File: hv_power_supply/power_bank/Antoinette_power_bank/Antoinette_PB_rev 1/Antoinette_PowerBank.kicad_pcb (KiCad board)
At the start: 2 copper layers, 30.5 x 48.3 mm, 44 parts, among them J1 NanoFit_RA_TH_02, J2 USB-Micro-1981568-1, J3 NanoFit_RA_TH_02, J4 USB-A-S-X-X-SM2, J5 NanoFit_RA_TH_02, Q1 SSM3K333R, U2 MCP73871T-2CCI_ML, U3 TPS61090RSAR

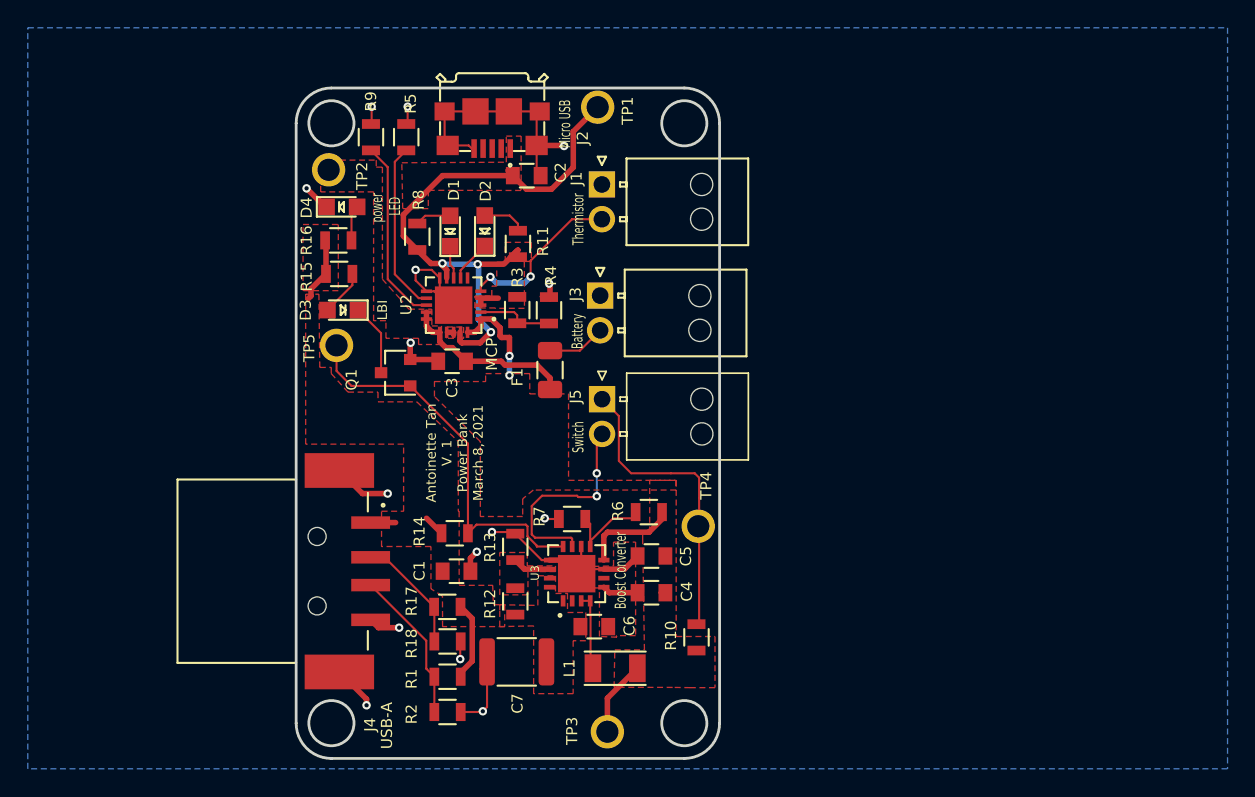
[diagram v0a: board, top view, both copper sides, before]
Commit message: UpdMoved USB-A in, and updated traces
Moved USB-A in, replaced copper pours with traces, added mounting holes
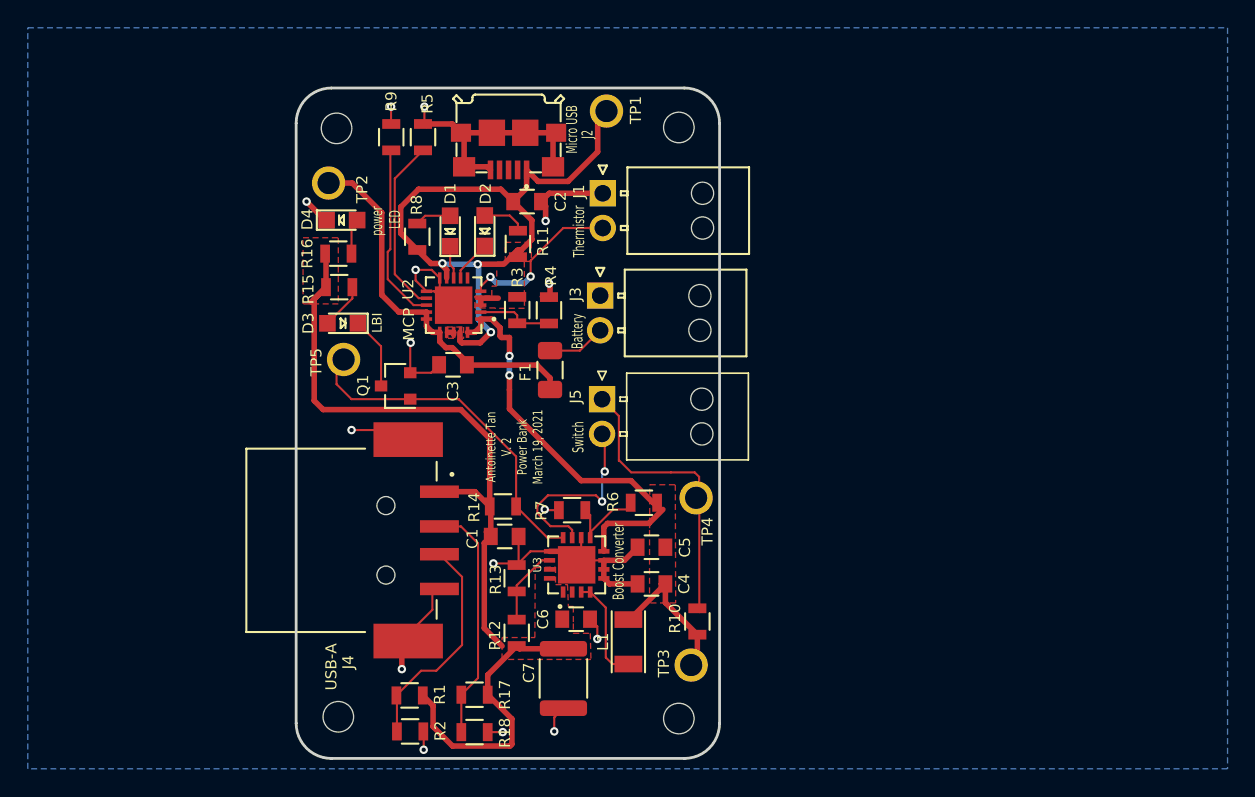
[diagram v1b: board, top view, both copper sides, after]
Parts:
- added R: MountingHole_2.2mm_M2, formula:MountingHole_2.2mm_M2, F.Cu at (97.7, 75.1)
- added REF**: MountingHole_2.2mm_M2, formula:MountingHole_2.2mm_M2, F.Cu at (73.2, 75.0)
- added REF**: MountingHole_2.2mm_M2, formula:MountingHole_2.2mm_M2, F.Cu at (97.7, 32.6)
- added REF**: MountingHole_2.2mm_M2, formula:MountingHole_2.2mm_M2, F.Cu at (73.0, 32.6)
- moved TP3 7.71 mm to (98.6, 71.3)
- moved R18 6.81 mm to (83.0, 76.1)
- moved R17 6.62 mm to (83.0, 73.4)
- moved J4 5.43 mm to (76.6, 62.3)
- moved C1 4.28 mm to (85.1, 62.0)
- moved R14 3.97 mm to (85.0, 59.9)
- moved C7 3.57 mm to (89.4, 72.2), turned to 270 degrees
- moved R1 3.04 mm to (78.3, 73.5)
- moved R2 3.03 mm to (78.3, 76.0)
- moved R13 2.26 mm to (86.0, 65.0)
- moved R12 2.26 mm to (86.0, 69.0)
- moved L1 2.13 mm to (94.0, 69.6), turned to 270 degrees
- moved TP4 2.05 mm to (98.9, 59.2)
- moved J2 1.94 mm to (85.4, 33.0)
- moved C2 1.87 mm to (86.7, 37.9)
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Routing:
- net +5V: track 15.9 -> 68.0 mm
- net +BATT: track 19.6 -> 40.1 mm
- net /Battery+: track 12.7 -> 26.9 mm
- net Net-(J4-Pad02): track 9.27 -> 18.9 mm
- net Net-(J4-Pad03): track 11.3 -> 17.6 mm
- net VBUS: track 44.4 -> 50.3 mm
- net GND: track 75.0 -> 80.5 mm
- net Net-(Q1-Pad1): track 28.1 -> 24.8 mm
- net Net-(R12-Pad2): track 2.74 -> 5.57 mm
- net Net-(L1-Pad2): track 4.93 -> 7.71 mm
- removed copper zone on F.Cu, net /Battery+
- removed copper zone on F.Cu, net GND
- removed copper zone on F.Cu, net Net-(R12-Pad2)
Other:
- outline, holes or cut-outs redrawn
- board text added: "Antoinette Tan V. 2 Power Bank March 19, 2021"
- board text removed: "Antoinette Tan V. 1 Power Bank March 8, 2021"

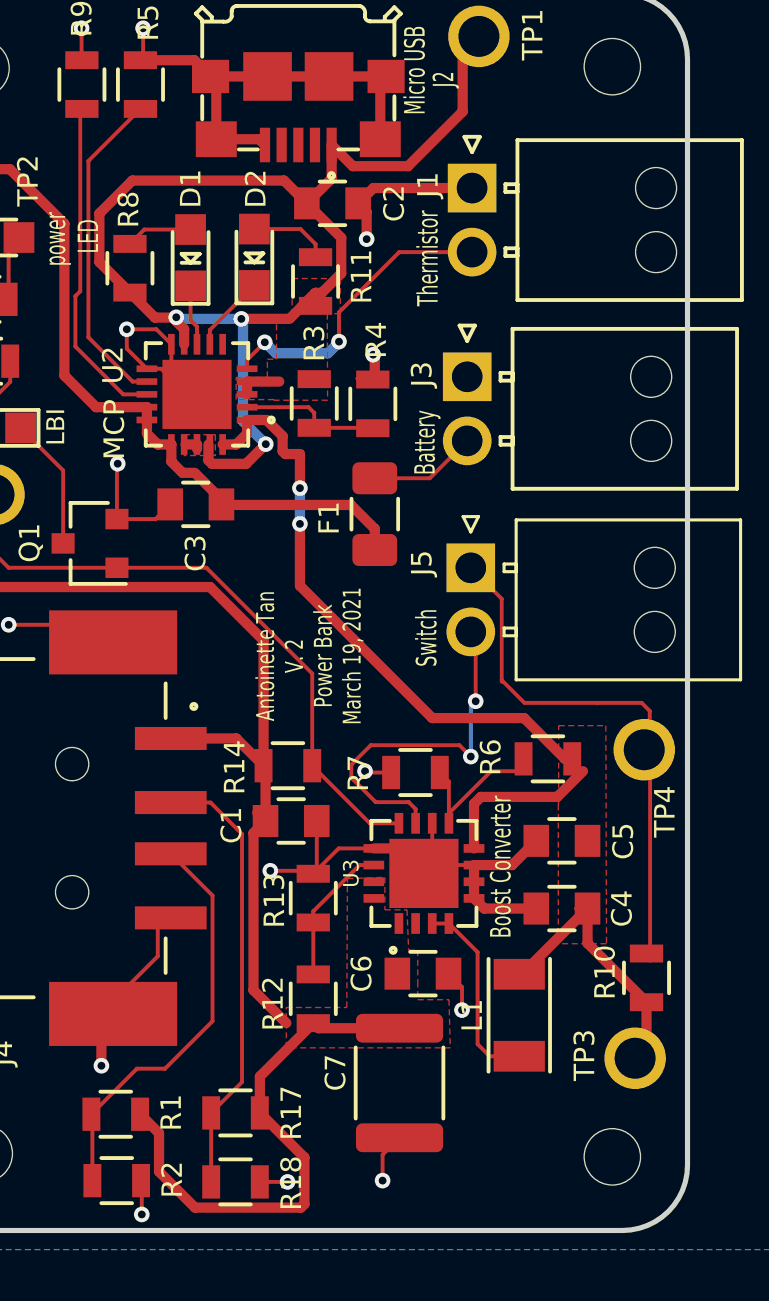
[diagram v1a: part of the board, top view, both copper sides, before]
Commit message: connect gnd to pw grnd
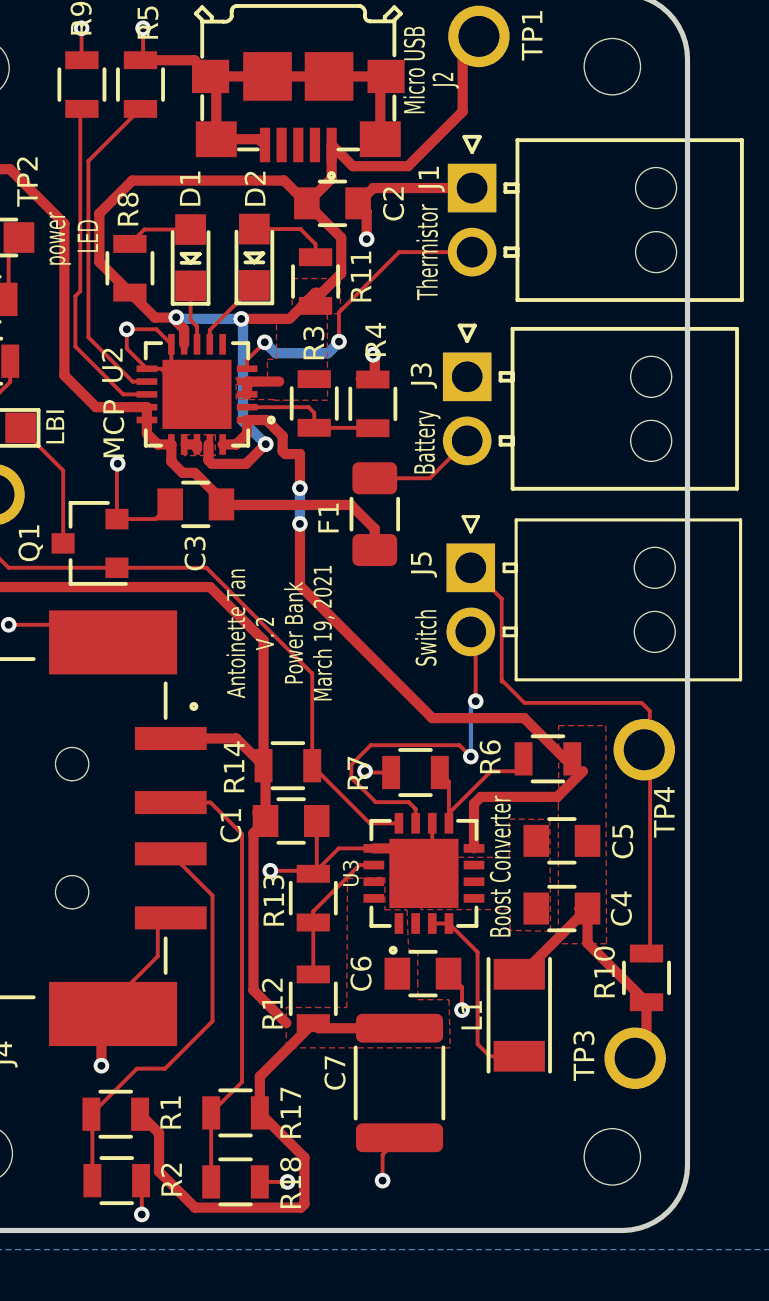
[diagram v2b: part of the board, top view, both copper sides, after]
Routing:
- net GND: track 80.5 -> 72.1 mm
- added copper zone on F.Cu, net GND

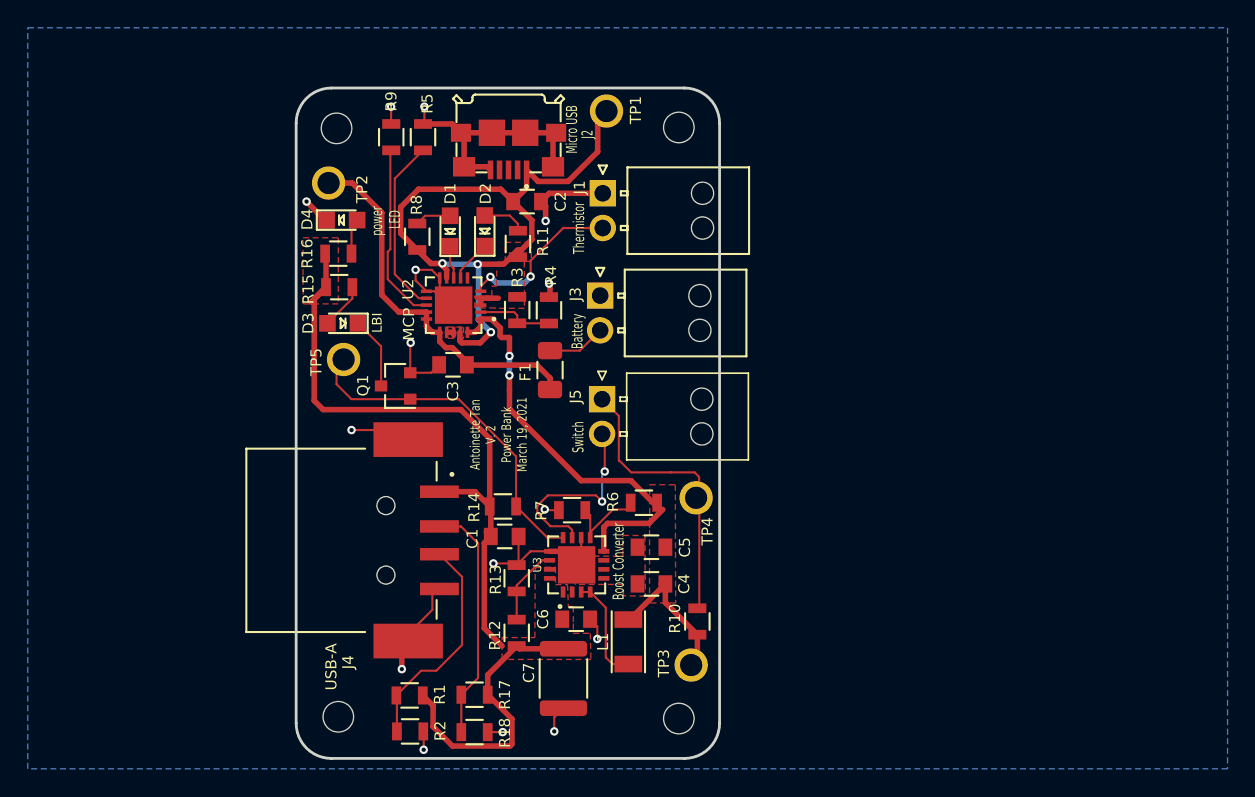
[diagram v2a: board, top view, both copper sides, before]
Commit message: Add updated PCB with new inductor.
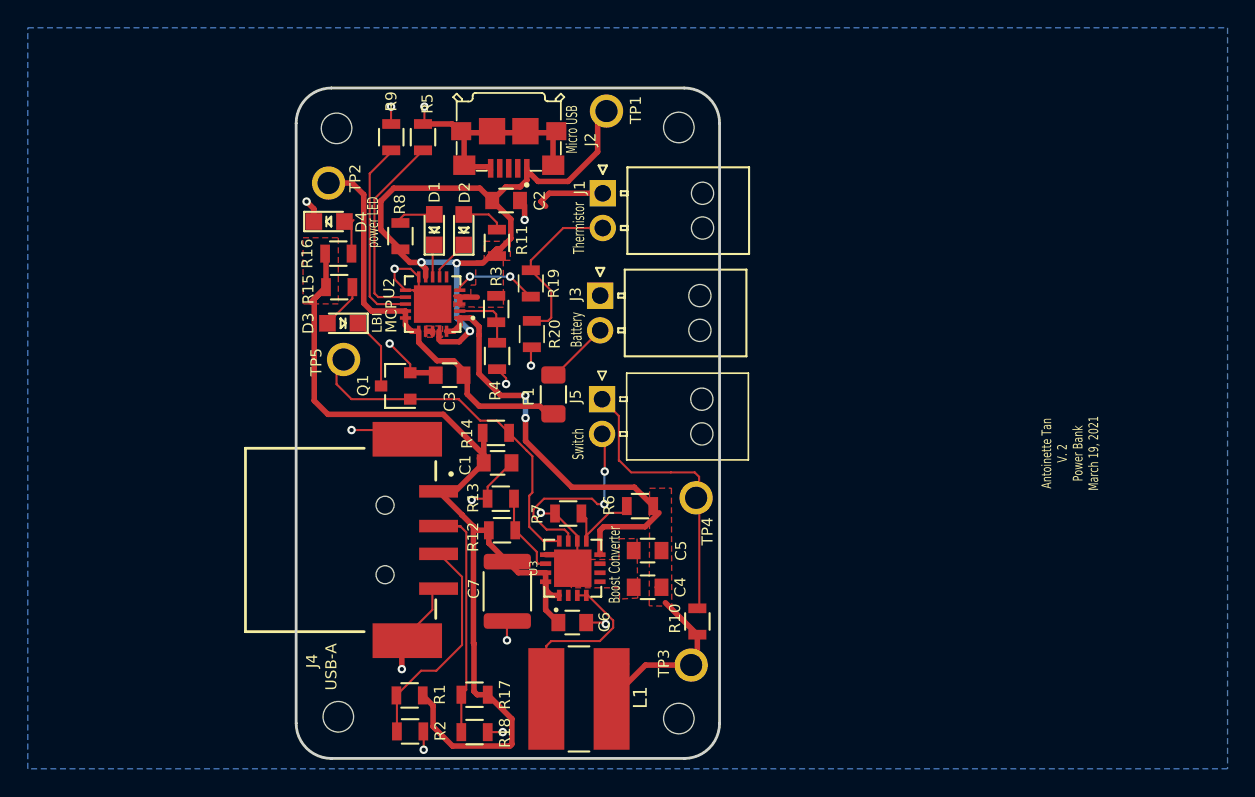
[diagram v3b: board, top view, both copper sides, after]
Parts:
- added R19: R_1.54K, footprints:R_0805_OEM, F.Cu at (87.0, 43.8)
- added R20: R_69.8K, footprints:R_0805_OEM, F.Cu at (87.1, 47.4)
- L1: value L_6.8uH -> L_10uH; footprint footprints:L_100uH_OEM -> footprints:BournsInductor
- moved C7 7.46 mm to (85.3, 66.0)
- moved R12 7.46 mm to (84.9, 61.6), turned to 0 degrees
- moved R13 5.84 mm to (84.8, 59.3), turned to 180 degrees
- moved L1 5.44 mm to (90.5, 73.7), turned to 0 degrees
- moved R14 5.32 mm to (84.5, 54.6)
- moved C1 5.32 mm to (84.6, 56.7)
- moved R4 4.97 mm to (84.6, 49.0), turned to 270 degrees
- moved F1 1.77 mm to (88.6, 51.8)
- moved C2 1.51 mm to (85.2, 37.8)
- moved R11 1.51 mm to (84.6, 40.9)
- moved U2 1.51 mm to (79.9, 45.3)
- moved D2 1.51 mm to (82.2, 39.9)
- moved R3 1.51 mm to (84.5, 45.6)
- moved R8 1.21 mm to (77.6, 40.4)
- moved D1 1.15 mm to (80.1, 39.9)
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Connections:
- J1 pad 2: /16KThermistor -> /10KThermistor
- L1 pad 1: +BATT -> Net-(L1-Pad1)
- L1 pad 2: Net-(L1-Pad2) -> +BATT
- U2 pad 5: /16KThermistor -> Net-(R19-Pad2)
- U3 pad 3: Net-(L1-Pad2) -> Net-(L1-Pad1)
- U3 pad 4: Net-(L1-Pad2) -> Net-(L1-Pad1)
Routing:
- net Net-(L1-Pad1): track 0.00 -> 13.1 mm
- net /10KThermistor: track 0.00 -> 12.4 mm
- net /16KThermistor: track 11.9 -> 0.00 mm, vias 2 -> 0
- net +5V: track 68.0 -> 76.1 mm
- net Net-(L1-Pad2): track 7.71 -> 0.00 mm
- net Net-(R19-Pad2): track 0.00 -> 6.38 mm, vias 0 -> 2
- net +BATT: track 40.1 -> 45.3 mm
- net /Battery+: track 26.9 -> 29.5 mm
- net GND: track 72.1 -> 73.5 mm, vias 15 -> 16
- net VBUS: track 50.3 -> 51.6 mm
- net Net-(R5-Pad1): track 12.8 -> 14.1 mm
- net Net-(R9-Pad1): track 12.9 -> 14.0 mm
- net Net-(Q1-Pad1): track 24.8 -> 25.8 mm
- net Net-(J4-Pad02): track 18.9 -> 19.8 mm
- net Net-(R3-Pad2): track 5.93 -> 5.14 mm
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
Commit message: Add new files for updated pcb.
Added files for updated pcb with new inductor and series/parallel resistors for the 10k thermistor.
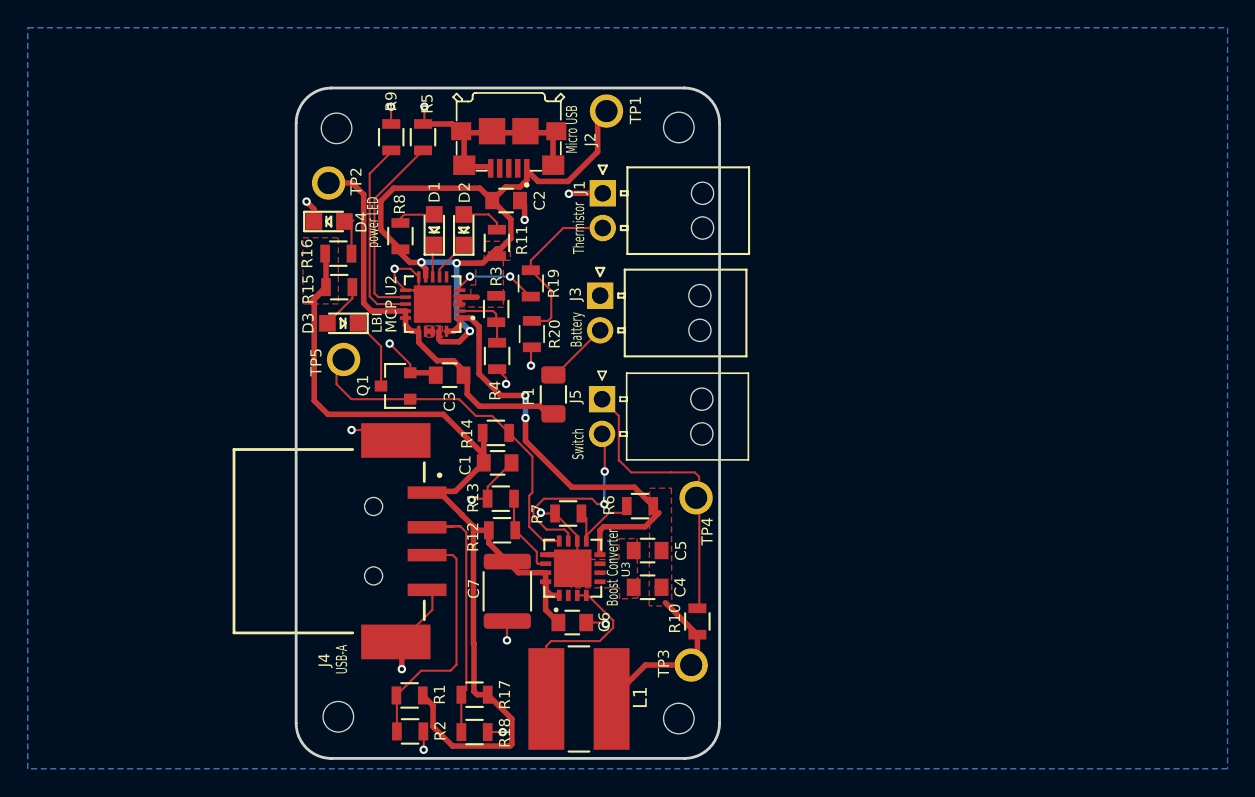
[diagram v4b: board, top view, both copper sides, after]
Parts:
- added G***: LOGO, footprints:Small_OE_Logo, B.Cu at (82.3, 42.2)
- moved J4 0.83 mm to (75.7, 62.4)
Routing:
- net GND: track 73.5 -> 68.6 mm, vias 16 -> 17
- net +BATT: track 45.3 -> 43.5 mm
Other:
- board text added: "Antoinette Tan Power Bank V. 3 March 19, 2021"
- board text removed: "Antoinette Tan V. 2 Power Bank March 19, 2021"

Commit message: Correct silkscreen date.
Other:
- board text added: "Antoinette Tan Power Bank V. 3 April 9th, 2021"
- board text removed: "Antoinette Tan Power Bank V. 3 March 19, 2021"
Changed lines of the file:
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@@
     (34 B.Paste user)
     (35 F.Paste user)
-    (36 B.SilkS user hide)
+    (36 B.SilkS user)
     (37 F.SilkS user)
     (38 B.Mask user hide)
@@
   )
   (setup
-    (last_trace_width 0.4)
+    (last_trace_width 0.1524)
     (user_trace_width 0.15)
     (user_trace_width 0.25)
@@
     (effects (font (size 0.8 0.5) (thickness 0.125)))
   )
-  (gr_text "Antoinette Tan\nPower Bank V. 3\nMarch 19, 2021\n" (at 95.8723 42.0751 90) (layer B.SilkS)
+  (gr_text "Antoinette Tan\nPower Bank V. 3\nApril 9th, 2021\n" (at 95.8723 42.0751 90) (layer B.SilkS)
     (effects (font (size 0.85 0.85) (thickness 0.2)) (justify mirror))
   )
